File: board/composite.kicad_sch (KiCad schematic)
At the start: 24 parts, among them J10 VGA, J5 JTAG BYPASS, J6 COMPOSITE, U17 OBVID, Y1 14.318MHz, Y3 25.175MHz

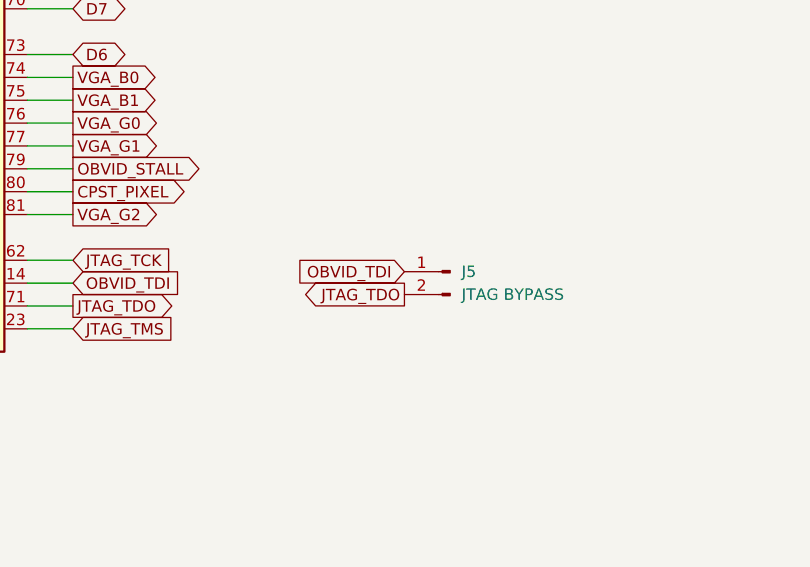
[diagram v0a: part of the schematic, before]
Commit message: update JTAG bypass and 8051 PS/2 pins
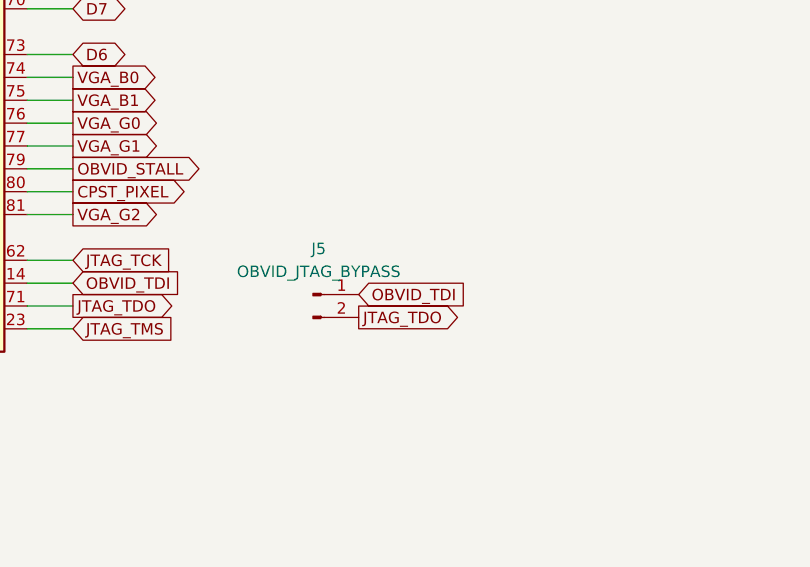
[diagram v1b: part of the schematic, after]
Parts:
- J5: value JTAG BYPASS -> OBVID_JTAG_BYPASS; footprint Connector_PinHeader_2.54mm:PinHeader_1x02_P2.54mm_Vertical -> (none)
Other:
- moved on the sheet: J5
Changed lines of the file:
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@@
 	(global_label "OBVID_TDI"
 		(shape input)
-		(at 137.16 161.29 180)
+		(at 132.08 163.83 0)
 		(fields_autoplaced yes)
 		(effects
@@
 				(size 1.27 1.27)
 			)
-			(justify right)
+			(justify left)
 		)
 		(property "Intersheetrefs" "${INTERSHEET_REFS}"
-			(at 125.6477 161.29 0)
+			(at 143.5923 163.83 0)
 			(effects
 				(font
 					(size 1.27 1.27)
 				)
-				(justify right)
+				(justify left)
 				(hide yes)
 			)
@@
 	(global_label "JTAG_TDO"
 		(shape output)
-		(at 137.16 163.83 180)
+		(at 132.08 166.37 0)
 		(fields_autoplaced yes)
 		(effects
@@
 				(size 1.27 1.27)
 			)
-			(justify right)
+			(justify left)
 		)
 		(property "Intersheetrefs" "${INTERSHEET_REFS}"
-			(at 125.3453 163.83 0)
+			(at 143.8947 166.37 0)
 			(effects
 				(font
 					(size 1.27 1.27)
 				)
-				(justify right)
+				(justify left)
 				(hide yes)
 			)
@@
 	(symbol
 		(lib_id "Connector:Conn_01x02_Pin")
-		(at 142.24 161.29 0)
-		(mirror y)
+		(at 127 163.83 0)
 		(unit 1)
 		(exclude_from_sim no)
@@
 		(fields_autoplaced yes)
 		(property "Reference" "J5"
-			(at 143.51 161.2899 0)
+			(at 127.635 158.75 0)
 			(effects
 				(font
 					(size 1.27 1.27)
 				)
-				(justify right)
 			)
 		)
-		(property "Value" "JTAG BYPASS"
-			(at 143.51 163.8299 0)
+		(property "Value" "OBVID_JTAG_BYPASS"
+			(at 127.635 161.29 0)
 			(effects
 				(font
 					(size 1.27 1.27)
 				)
-				(justify right)
 			)
 		)
-		(property "Footprint" "Connector_PinHeader_2.54mm:PinHeader_1x02_P2.54mm_Vertical"
-			(at 142.24 161.29 0)
+		(property "Footprint" ""
+			(at 127 163.83 0)
 			(effects
 				(font
@@
 		)
 		(property "Datasheet" "~"
-			(at 142.24 161.29 0)
+			(at 127 163.83 0)
 			(effects
 				(font
@@
 		)
 		(property "Description" "Generic connector, single row, 01x02, script generated"
-			(at 142.24 161.29 0)
+			(at 127 163.83 0)
 			(effects
 				(font

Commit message: JTAG bypass, GLUE A18, OBVID pins
Fix up JTAG bypass again
Switch GLUE A6 to GLUE A18
Clean up some OBVID pins
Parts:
- J5: footprint (none) -> Connector_PinHeader_2.54mm:PinHeader_1x02_P2.54mm_Vertical
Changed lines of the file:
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@@
 			)
 		)
-		(property "Footprint" ""
+		(property "Footprint" "Connector_PinHeader_2.54mm:PinHeader_1x02_P2.54mm_Vertical"
 			(at 127 163.83 0)
 			(effects

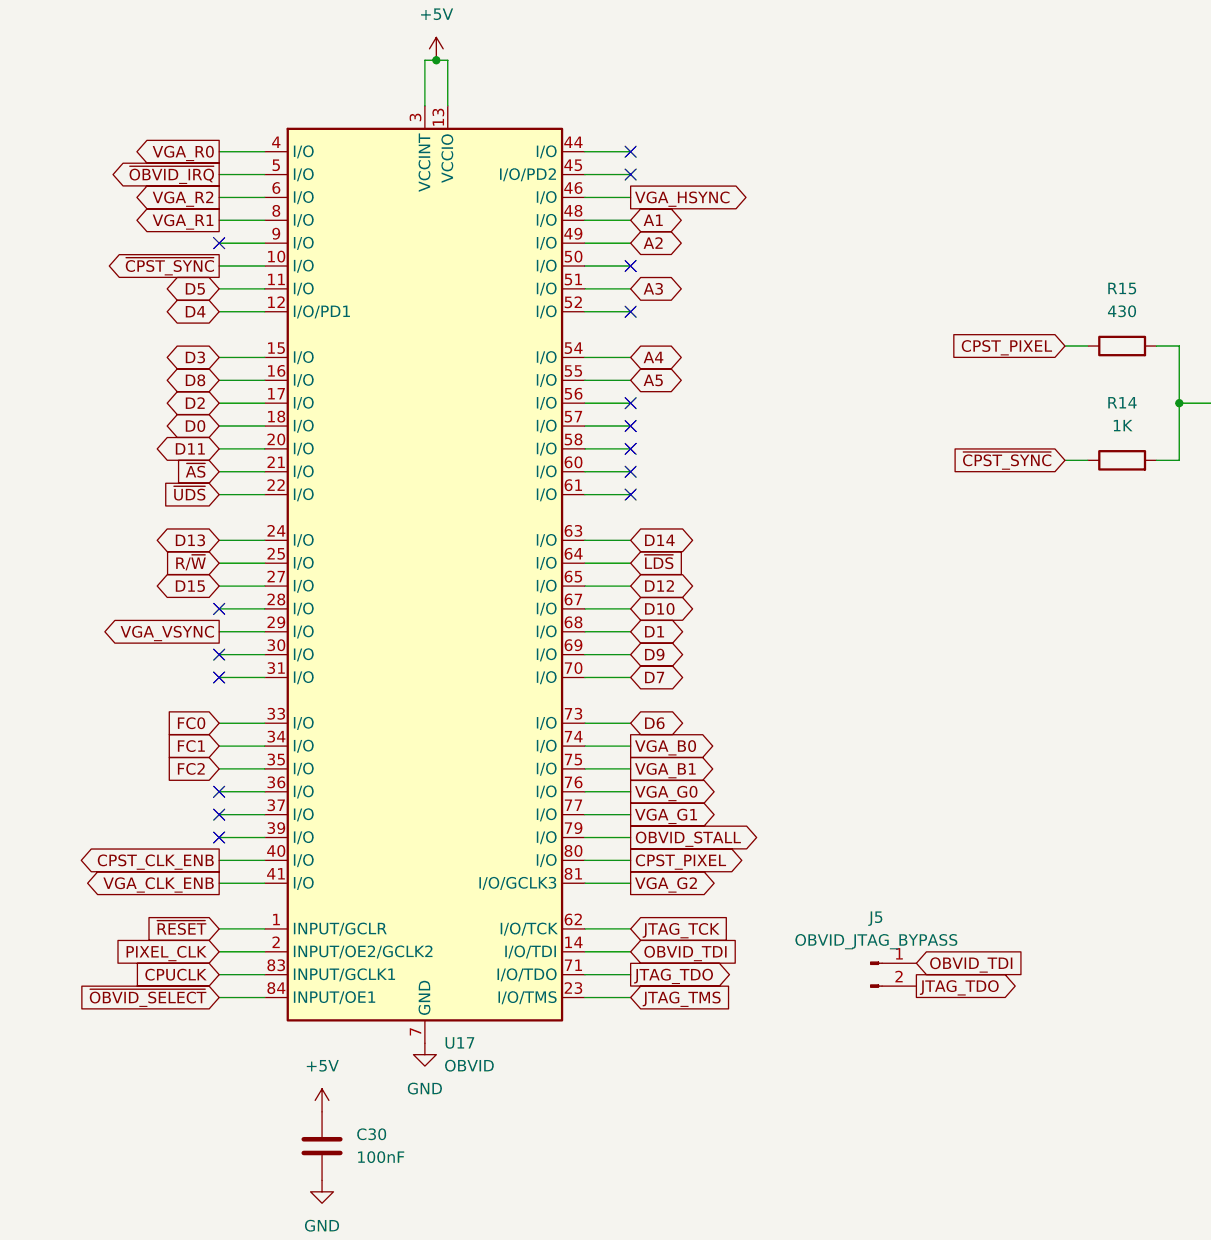
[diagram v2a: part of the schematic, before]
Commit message: change OBVID to VIDEO
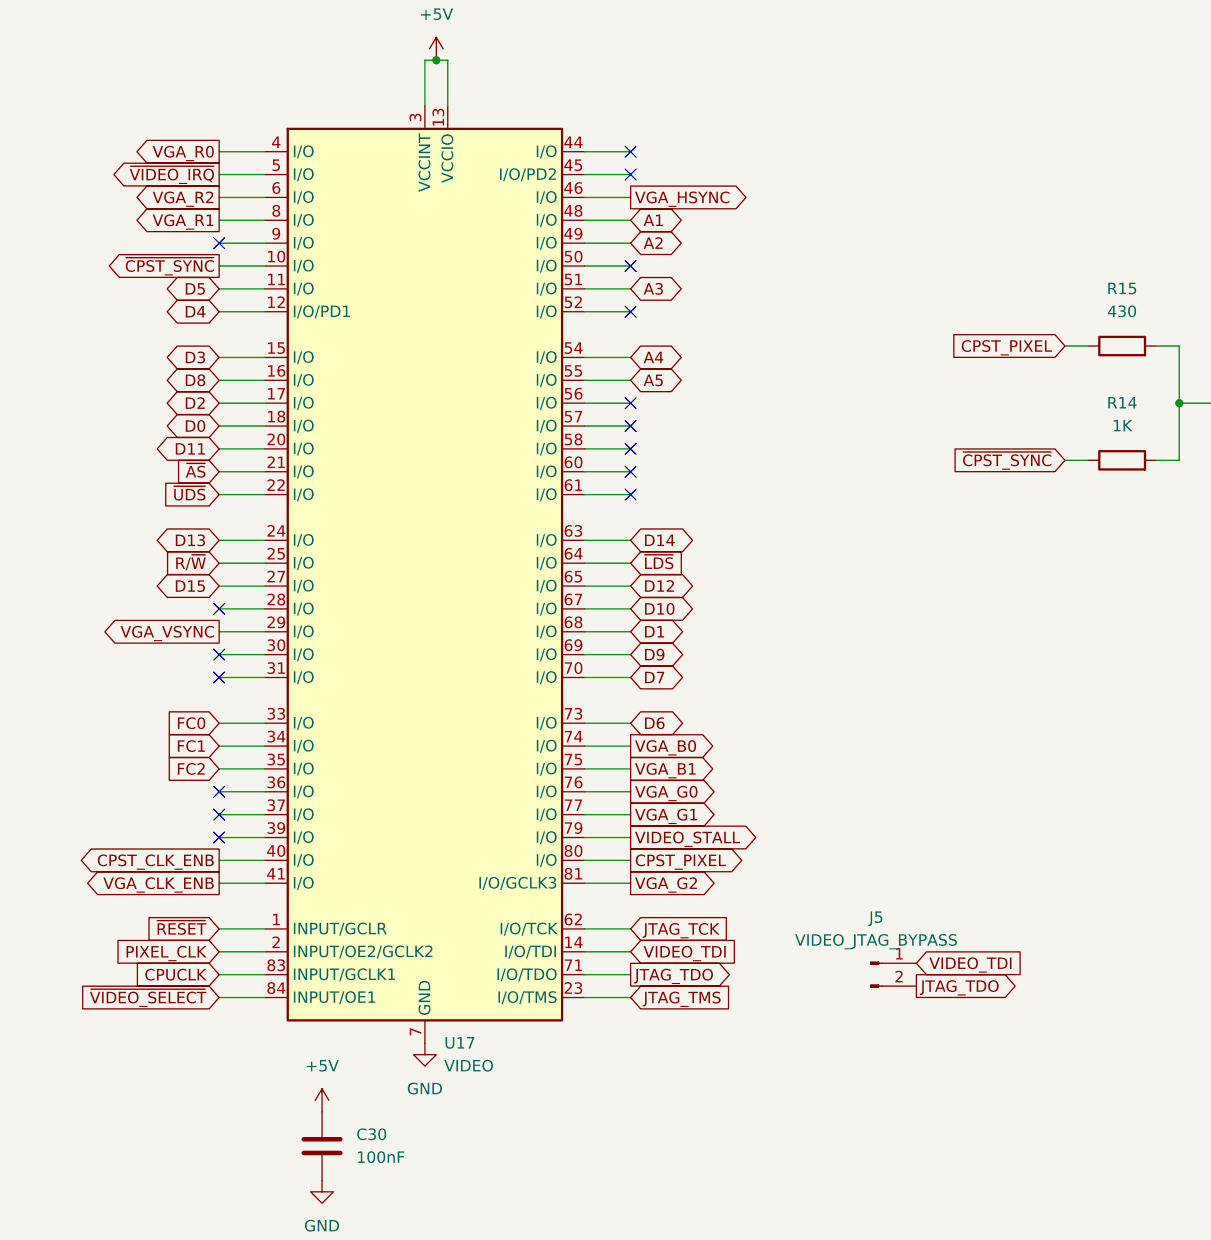
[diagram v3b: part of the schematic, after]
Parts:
- J5: value OBVID_JTAG_BYPASS -> VIDEO_JTAG_BYPASS
- U17: value OBVID -> VIDEO
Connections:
- net OBVID_STALL renamed VIDEO_STALL
- net OBVID_TDI renamed VIDEO_TDI
- net ~{OBVID_IRQ} renamed ~{VIDEO_IRQ}
- net ~{OBVID_SELECT} renamed ~{VIDEO_SELECT}
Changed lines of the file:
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@@
 		)
 	)
-	(global_label "OBVID_TDI"
+	(global_label "VIDEO_TDI"
 		(shape input)
 		(at 132.08 163.83 0)
@@
 		)
 	)
-	(global_label "OBVID_TDI"
+	(global_label "VIDEO_TDI"
 		(shape input)
 		(at 100.33 162.56 0)
@@
 		)
 	)
-	(global_label "~{OBVID_IRQ}"
+	(global_label "~{VIDEO_IRQ}"
 		(shape output)
 		(at 54.61 76.2 180)
@@
 		)
 	)
-	(global_label "~{OBVID_SELECT}"
+	(global_label "~{VIDEO_SELECT}"
 		(shape input)
 		(at 54.61 167.64 180)
@@
 		)
 	)
-	(global_label "OBVID_STALL"
+	(global_label "VIDEO_STALL"
 		(shape output)
 		(at 100.33 149.86 0)
@@
 			)
 		)
-		(property "Value" "OBVID"
+		(property "Value" "VIDEO"
 			(at 79.6133 175.26 0)
 			(effects
@@
 			)
 		)
-		(property "Value" "OBVID_JTAG_BYPASS"
+		(property "Value" "VIDEO_JTAG_BYPASS"
 			(at 127.635 161.29 0)
 			(effects

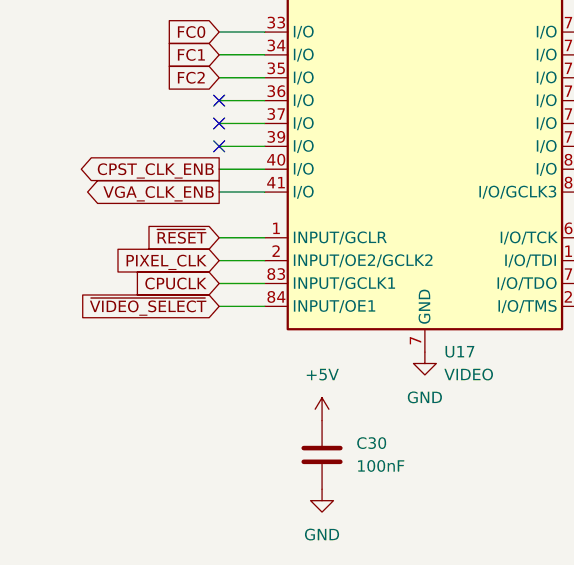
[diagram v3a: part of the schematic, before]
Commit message: CPUCLK -> SYSCLK
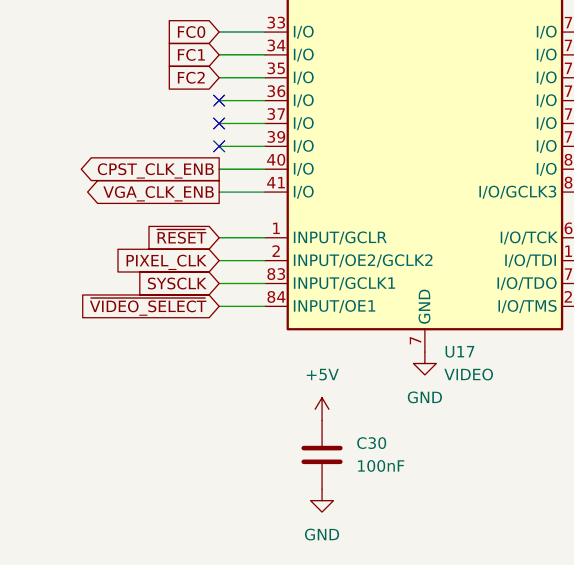
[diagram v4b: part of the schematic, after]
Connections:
- net CPUCLK renamed SYSCLK
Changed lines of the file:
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@@
 		)
 	)
-	(global_label "CPUCLK"
+	(global_label "SYSCLK"
 		(shape input)
 		(at 54.61 165.1 180)
